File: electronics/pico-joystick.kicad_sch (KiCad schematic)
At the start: 15 parts, among them J1 Gameport socket, J2 Gameport plug, J3 Serial, J4 Debug, SW1 SW_SPST, SW2 SW_SPST, U1 Raspberry Pi Pico

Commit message: Corrected PCB design
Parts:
- removed J1: Gameport socket, Connector_Dsub:DSUB-15_Female_Horizontal_P2.77x2.84mm_EdgePinOffset9.90mm_Housed_MountingHolesOffset11.32mm, symbol Connector:DA15_Receptacle
- added J1: Gameport socket, Connector_Dsub:DSUB-15_Female_Horizontal_P2.77x2.84mm_EdgePinOffset9.90mm_Housed_MountingHolesOffset11.32mm, symbol Connector:DA15_Receptacle_MountingHoles
- renumbered Axis2 to Axis1, Axis1 to Axis2, J4 to J2, J2 to J4, R3 to R1, R4 to R2, R1 to R3, R2 to R4
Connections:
- net +3V3: now also J1.1
- net GND: now also U1.13 (GND), U1.18 (GND), U1.23 (GND), U1.28 (GND), U1.3 (GND), U1.33 (GND), U1.8 (GND), J1.0 (PAD), J1.4
- net at R4.1, U1.32 (GP27): now also J1.6
- net at R3.1, U1.31 (GP26): now also J1.3
- net at R1.1: now also J1.2
- net at R2.1: now also J1.7
- no-connect marks 54 -> 47
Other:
- moved on the sheet: J2, J3, R3, R4

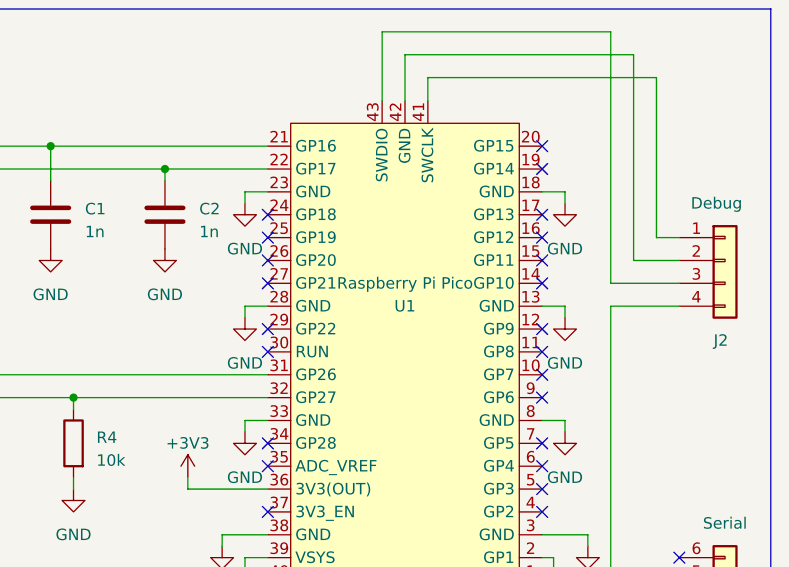
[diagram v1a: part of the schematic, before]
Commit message: Fixed overlapping text
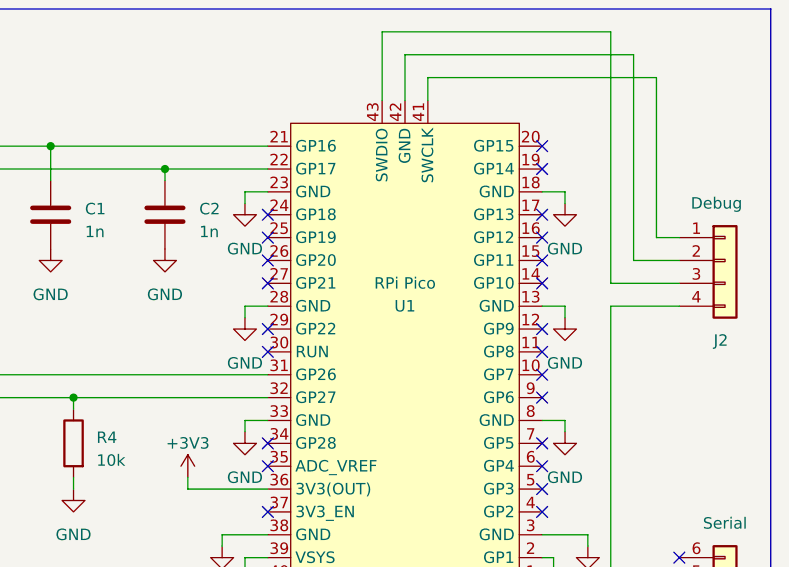
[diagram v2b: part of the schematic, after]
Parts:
- U1: value Raspberry Pi Pico -> RPi Pico
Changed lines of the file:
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@@
       (effects (font (size 1.27 1.27)))
     )
-    (property "Value" "Raspberry Pi Pico" (at 196.85 80.01 0)
+    (property "Value" "RPi Pico" (at 196.85 80.01 0)
       (effects (font (size 1.27 1.27)))
     )
